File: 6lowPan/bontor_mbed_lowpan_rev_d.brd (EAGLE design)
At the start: 98 x 107 mm, 170 parts, among them IC1 SIM900, IC2 74HC595D, IC3 74HC595D, IC4 ADE7758RW, IC5 74HC595D, J1 U.FL, U2 W5500, X1 NX2520SA

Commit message: add gerber and BoM
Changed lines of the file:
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@@
 <setting verticaltext="up"/>
 </settings>
-<grid distance="0.1" unitdist="mm" unit="mm" style="lines" multiple="1" display="yes" altdistance="0.125" altunitdist="mm" altunit="mm"/>
+<grid distance="1" unitdist="mm" unit="mm" style="lines" multiple="1" display="yes" altdistance="0.125" altunitdist="mm" altunit="mm"/>
 <layers>
 <layer number="1" name="Top" color="4" fill="1" visible="yes" active="yes"/>
@@
 <polygon width="0.254" layer="1" isolate="0.4064">
 <vertex x="40.25" y="107"/>
-<vertex x="68.25" y="107"/>
-<vertex x="68.25" y="69.75"/>
-<vertex x="40.25" y="69.75"/>
+<vertex x="70.25" y="107"/>
+<vertex x="70.25" y="69.35"/>
+<vertex x="40.25" y="69.35"/>
 </polygon>
 <via x="58.75" y="76" extent="1-16" drill="0.4"/>
@@
 <via x="36.275" y="93.675" extent="1-16" drill="0.5"/>
 <wire x1="36.275" y1="93.675" x2="36.275" y2="93.35" width="1.016" layer="1"/>
-<wire x1="57.25" y1="70.4" x2="53.95" y2="70.375" width="0" layer="19" extent="1-1"/>
 </signal>
 <signal name="VDD">
@@
 <wire x1="65" y1="73.75" x2="65" y2="74.4" width="0.4064" layer="16"/>
 <wire x1="60.25" y1="72.475" x2="60.25" y2="70.95" width="0.5" layer="1"/>
-<wire x1="60.25" y1="70.95" x2="60.9" y2="70.3" width="0.5" layer="1"/>
-<wire x1="60.9" y1="70.3" x2="64.4" y2="70.3" width="0.5" layer="1"/>
-<wire x1="64.4" y1="70.3" x2="65" y2="70.9" width="0.5" layer="1"/>
 <wire x1="65" y1="70.9" x2="65" y2="73.75" width="0.5" layer="1"/>
+<wire x1="60.25" y1="70.95" x2="60.7" y2="70.5" width="0.5" layer="1"/>
+<wire x1="60.7" y1="70.5" x2="64.6" y2="70.5" width="0.5" layer="1"/>
+<wire x1="64.6" y1="70.5" x2="65" y2="70.9" width="0.5" layer="1"/>
 </signal>
 <signal name="N$8">

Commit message: update all PCB design
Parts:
- removed SENSOR-DHT: PINHD4, TFT_LCD_2.2:PINHD4
- added U$17: (no value), DHT11:DHT11
- RTO1, RTO2, RTO3: device rcl:0309/12 -> rcl:0309_12
- SR_OUT1, SR_OUT2: device pinhead:2X05/90 -> pinhead:2X05
- moved PWR-SWT 33.8 mm to (35.6, 72.4), turned to 270 degrees
- moved U$6 31.5 mm to (21.3, 66.1), flipped to the top
- moved SIM900-T3 8.61 mm to (45.7, 96.8), flipped to the bottom, turned to 180 degrees
- moved SR_OUT1 5.29 mm to (35.2, 6.90), flipped to the bottom, turned to 0 degrees
- moved SR_OUT2 5.29 mm to (56.1, 6.90), flipped to the bottom, turned to 0 degrees
- moved ADE-R8 4.85 mm to (40.5, 62.6)
- moved MQ2-R1 4.39 mm to (69.5, 62.6)
- moved SENSOR-MQ2 4.28 mm to (66.6, 63.4)
- moved SIM900-R10 3.73 mm to (42.2, 97.9), flipped to the bottom
- moved ADE-R16 3.52 mm to (21.3, 60.8), turned to 270 degrees
- moved SYS-C4 2.55 mm to (29.0, 73.2), flipped to the bottom
- moved ADE-R14 2.28 mm to (23.9, 62.9), turned to 0 degrees
- moved SYS-R2 1.80 mm to (32.5, 73.4), flipped to the bottom, turned to 0 degrees
- moved SYS-L1 1.68 mm to (32.6, 71.0), flipped to the bottom, turned to 180 degrees
- moved SYS-C1 1.67 mm to (45.1, 63.4)
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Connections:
- new net N$45: STM_CHIP.60
- net CH1_A: now also JP1.1; no longer JP1.2
- net CH1_B: now also JP1.2; no longer JP1.1
- net CH2_A: now also JP1.3; no longer JP1.4
- net CH2_B: now also JP1.4; no longer JP1.3
- net CH3_A: now also JP1.5; no longer JP1.6
- net CH3_B: now also JP1.6; no longer JP1.5
- net CH4_A: now also JP1.7; no longer JP1.8
- net CH4_B: now also JP1.8; no longer JP1.7
- net DGND: now also U$17.GND; no longer SENSOR-DHT.4
- net DHT_DATA: now also U$17.DATA; no longer SENSOR-DHT.2
- net VDD: now also U$17.VCC; no longer SENSOR-DHT.1
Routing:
- net +5V: track 234.7 -> 258.1 mm
- net VCC: track 232.3 -> 241.6 mm, vias 10 -> 11
- net Q15: track 16.3 -> 8.55 mm
- net DGND: track 438.1 -> 431.2 mm, vias 71 -> 73
- net Q13: track 22.3 -> 16.2 mm
- net Q11: track 28.6 -> 22.8 mm
- net Q7: track 22.2 -> 16.5 mm
- net SIM_PWRKEY: track 81.5 -> 86.7 mm, vias 4 -> 5
- net VDD: track 565.3 -> 570.1 mm, vias 24 -> 25
- net Q9: track 42.2 -> 37.4 mm
- net N$40: track 44.6 -> 40.1 mm
- net AGND: track 196.3 -> 192.0 mm, vias 18 -> 16
- net N$48: track 26.8 -> 30.8 mm, vias 3 -> 1
- net Q16: track 9.17 -> 5.48 mm
- net Q5: track 25.9 -> 22.2 mm
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
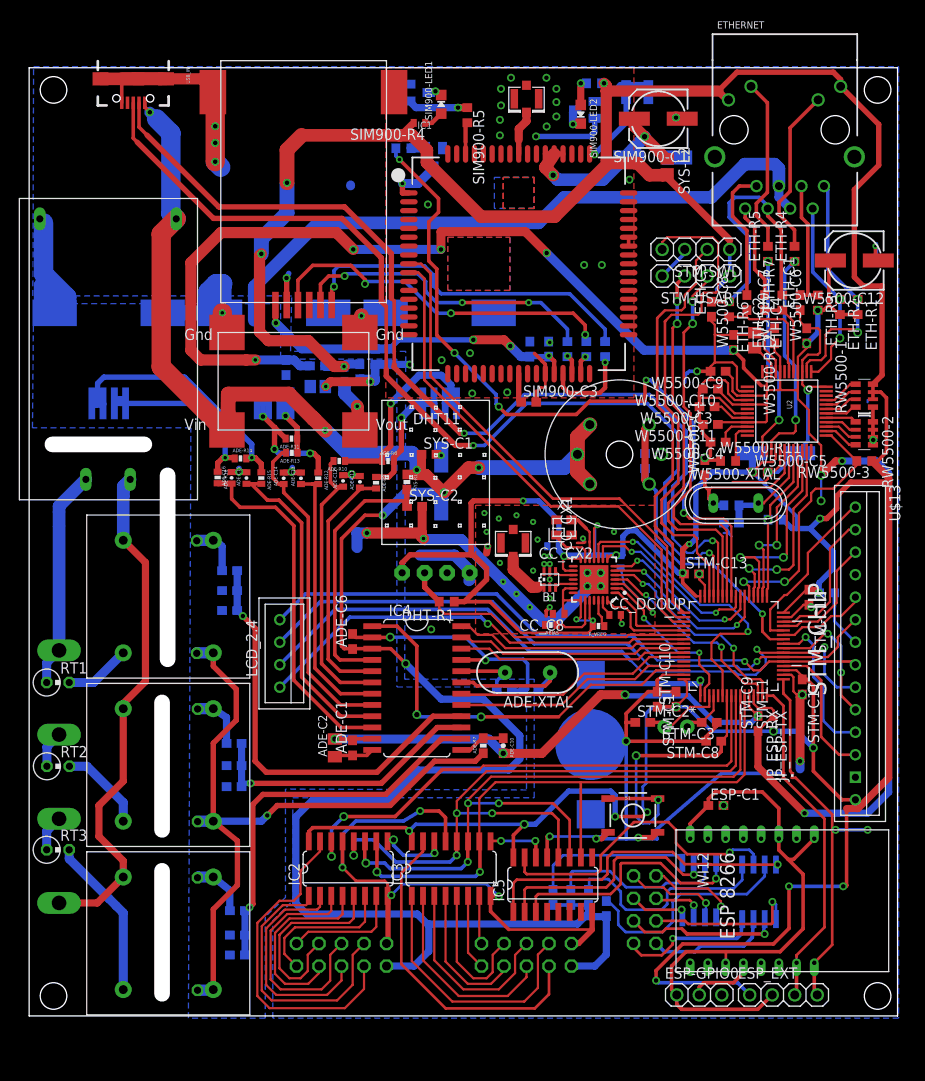
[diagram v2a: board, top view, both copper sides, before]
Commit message: adding designators and center components on its origin
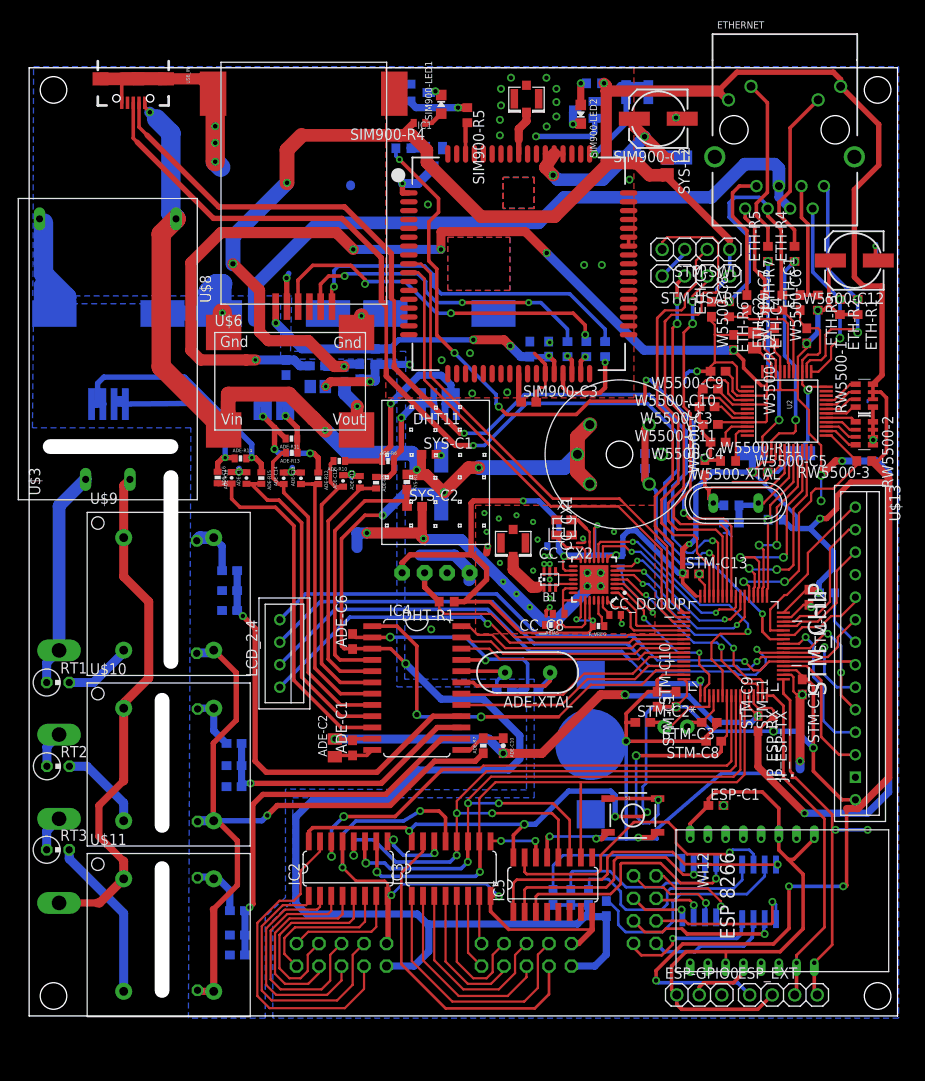
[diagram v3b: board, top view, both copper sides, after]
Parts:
- moved U$3 19.8 mm to (8.88, 75.2)
- moved U$8 17.2 mm to (31.0, 94.9)
- moved U$9 13.3 mm to (15.8, 47.6)
- moved U$10 13.1 mm to (15.8, 28.4)
- moved U$11 12.9 mm to (15.8, 9.12)
- moved U$14 11.4 mm to (46.3, 79.0)
- moved U$15 11.4 mm to (27.6, 79.0)
- moved U$16 11.4 mm to (8.95, 79.0)
- moved U$6 9.81 mm to (29.4, 71.6)
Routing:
- net VDD: track 570.1 -> 572.6 mm
- net N$55: track 81.9 -> 82.5 mm
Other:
- outline, holes or cut-outs redrawn
